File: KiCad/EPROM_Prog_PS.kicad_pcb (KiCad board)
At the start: 2 copper layers, 39.5 x 56.5 mm, 25 parts, among them J1 13Vdc_In, J2 Prog_EN, J3 Vpp_Vcc_Out, Q1 SST3904, Q2 TM2301GN, U1 LM317L_TO92

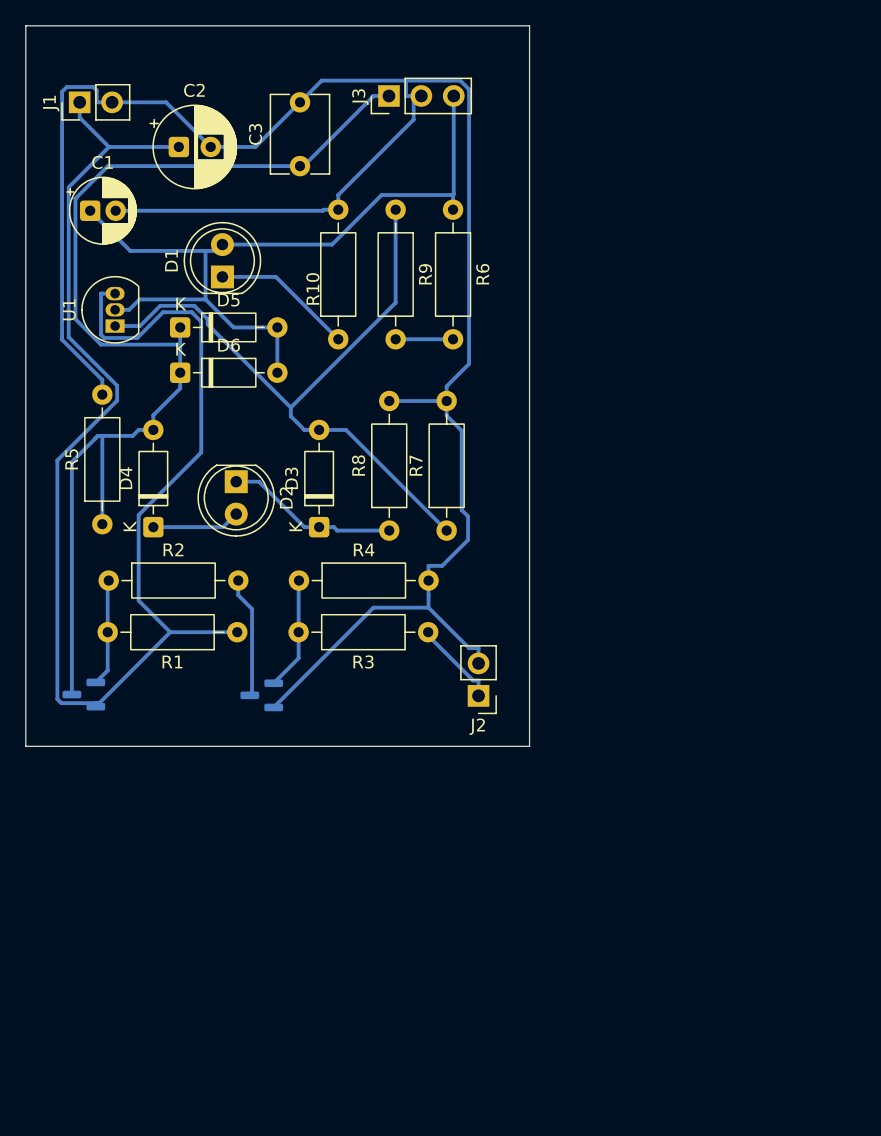
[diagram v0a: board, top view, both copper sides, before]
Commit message: PCB: increased dimension
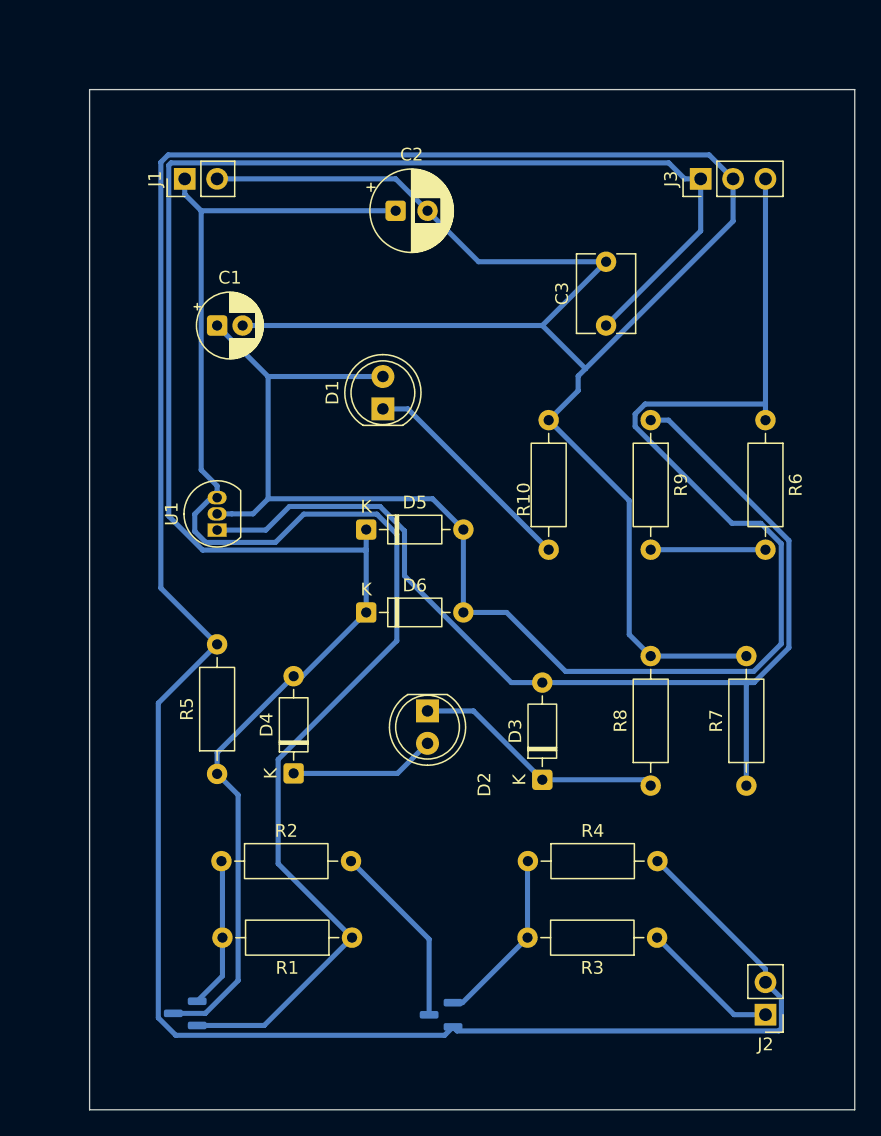
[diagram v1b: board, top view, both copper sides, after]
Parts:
- moved J2 33.6 mm to (73.0, 92.5)
- moved R7 30.9 mm to (71.5, 74.6)
- moved R3 29.9 mm to (64.5, 86.5)
- moved R6 29.5 mm to (73.0, 45.9)
- moved Q1 28.7 mm to (47.6, 92.5)
- moved R8 28.6 mm to (64.0, 74.6)
- moved R4 28.4 mm to (54.4, 80.5)
- moved C3 27.1 mm to (60.5, 38.5)
- moved D3 26.4 mm to (55.5, 74.1)
- moved Q2 26.2 mm to (27.5, 92.4)
- moved R9 25.9 mm to (64.0, 45.9)
- moved R1 25.6 mm to (40.6, 86.5)
- moved J3 25.3 mm to (67.9, 27.0)
- moved D6 23.8 mm to (41.7, 61.0)
- moved R2 23.7 mm to (30.3, 80.5)
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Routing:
- net GND: track 163.6 -> 306.6 mm
- net Net-(D1-A): track 61.8 -> 132.8 mm
- net Net-(D4-A): track 88.2 -> 148.4 mm
- net Net-(D3-A): track 53.5 -> 85.7 mm
- net Net-(D1-K): track 11.1 -> 17.6 mm
- net Net-(D2-K): track 13.6 -> 19.9 mm
- net Net-(Q1-B): track 8.87 -> 14.0 mm
- net Net-(Q1-C): track 9.52 -> 14.6 mm
- net Net-(D2-A): track 6.92 -> 11.5 mm
- net Net-(R6-Pad2): track 4.50 -> 9.00 mm
- net Net-(J2-Pin_1): track 6.87 -> 11.0 mm
- net Net-(Q2-G): track 8.41 -> 11.8 mm
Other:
- board size 39.5 x 56.5 mm -> 60 x 80 mm
